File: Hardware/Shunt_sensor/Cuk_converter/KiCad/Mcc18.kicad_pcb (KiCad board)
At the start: 2 copper layers, 177.8 x 104.1 mm, 89 parts, among them Q1 IRFP4321PbF, U1 INA240, U2 DRIVER_(INEP), U3 LM7812_TO220, U4 Signals_MCC, U5 ZCS

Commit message: Finalized first version PCB
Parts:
- removed JP2: MosfetOn, Jumper:SolderJumper-2_P1.3mm_Open_TrianglePad1.0x1.5mm
- removed JP3: Diode On, Jumper:SolderJumper-2_P1.3mm_Open_Pad1.0x1.5mm
- removed Rg2: 10k, Resistor_SMD:R_0805_2012Metric_Pad1.15x1.40mm_HandSolder
- added JP5: ON/OFF, TerminalBlock:TerminalBlock_bornier-2_P5.08mm, F.Cu at (53.8, 40.6)
- added TP13: TP, TestPoint:TestPoint_Pad_2.0x2.0mm, B.Cu at (196.1, 145.3)
- added TP14: TP, TestPoint:TestPoint_Pad_2.0x2.0mm, F.Cu at (146.8, 113.3)
- C1: footprint Capacitor_SMD:C_0805_2012Metric_Pad1.15x1.40mm_HandSolder -> Capacitor_SMD:C_2512_6332Metric_Pad1.52x3.35mm_HandSolder; moved to B.Cu
- Cc10, Cc11, Cc12, Cc7, Cc8, Cc9, Ci1, Ci2, Ci3, Co1, Co2, Co3, Co4, Co5, HS1, L1/2, L2/2, Q1, R110, Tvs1, Tvs2, Tvs4, U1: moved to B.Cu
- Cs12, Cs13, Cs14, Cs15, Ds1, Ds2, Ds3, Ds4, F1, JP4, R103, R105, Rs2, Rs3, Rs4, Rs5: moved to F.Cu
- D1: footprint MCCplaca:TO-247-3_Horizontal_TabUp -> Package_TO_SOT_THT:TO-247-3_Horizontal_TabUp; moved to B.Cu
- JP1: value Diode On -> VBat-Sen
- L1, L3: footprint Inductor_SMD:L_0805_2012Metric_Pad1.15x1.40mm_HandSolder -> Jumper:SolderJumper-2_P1.3mm_Open_Pad1.0x1.5mm
- Rshunt1: footprint MCCplaca Shunt:PML100HZPJV0L5 -> MCCplaca:PML100HZPJV0L5; moved to B.Cu
- TP1, TP10, TP11, TP12, TP2, TP3, TP4, TP6, TP7, TP8, TP9: value TestPoint_Probe -> TP; footprint TestPoint:TestPoint_Pad_D1.0mm -> TestPoint:TestPoint_Pad_2.0x2.0mm
- TP5: value TestPoint_Probe -> TP; footprint TestPoint:TestPoint_Pad_D1.0mm -> TestPoint:TestPoint_Pad_2.0x2.0mm; moved to B.Cu
- U2: footprint MCCplaca:Driver_(INEP)_SMD -> MCCplaca:Driver_(INEP); moved to F.Cu
- U3: footprint MCCplaca:TO-220-3_Horizontal_TabDown_SMD -> MCCplaca:TO-220-3_Horizontal_TabDown; moved to F.Cu
- U4: footprint MCCplaca:SignalsBarrapinos_SMD -> MCCplaca:SignalsBarrapinosGrande; moved to B.Cu
- U5: footprint MCCplaca:ZCS18 -> MCCplaca:ZCS18_Handsoldering
- moved Tvs1 233.7 mm to (88.3, 57.8), turned to 180 degrees
- moved R105 225.5 mm to (184.8, 67.9), turned to 90 degrees
- moved JP4 224.1 mm to (188.0, 69.2), turned to 0 degrees
- moved Tvs2 223.4 mm to (89.9, 54.3)
- moved R102 222.4 mm to (188.0, 120.1), turned to 180 degrees
- moved C1 221.9 mm to (102.2, 49.5), turned to 90 degrees
- moved R103 221.3 mm to (187.5, 65.5), turned to 180 degrees
- moved R110 221.0 mm to (106.0, 52.6)
- moved R101 220.0 mm to (188.0, 123.4), turned to 180 degrees
- moved Tvs4 209.6 mm to (108.7, 102.2), turned to 90 degrees
- moved TP8 143.6 mm to (105.4, 112.4)
- moved TP12 135.8 mm to (177.2, 109.9)
- moved TP10 134.6 mm to (173.4, 113.0)
- moved TP9 132.7 mm to (110.5, 106.0)
- moved TP11 126.9 mm to (160.7, 104.8)
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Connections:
- net /HG renamed /Gate
- net /HS renamed /Source
- net Net-(F1-Pad2) renamed /-P_unfused
- C11 pad 1: GND -> GNDA
- C16 pad 2: GND -> GNDA
- D1 pad 1: Net-(D1-Pad1) -> /-B
- JP1 pad 1: Net-(D1-Pad1) -> /-B
- JP1 pad 2: /-B -> GND
- Tvs3 pad 2: GND -> GNDA
- U1 pad 2: GND -> GNDA
- U2 pad 3: /LG -> Net-(U2-Pad3)
- U2 pad 4: /-B -> GND
- U5 pad 2: Net-(U5-Pad2) -> GND
- U5 pad 4: Net-(U5-Pad4) -> GND
- U5 pad 6: Net-(U5-Pad6) -> GND
- U5 pad 8: Net-(U5-Pad8) -> GND
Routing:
- net /+Vp: track 506.7 -> 34.7 mm, vias 0 -> 1
- net /+B: track 425.0 -> 27.9 mm, vias 1 -> 5
- net /-B: track 472.2 -> 128.7 mm, vias 0 -> 1
- net GND: track 551.4 -> 236.3 mm, vias 4 -> 15
- net +5VA: track 17.0 -> 262.4 mm, vias 1 -> 3
- net /-Vp: track 248.7 -> 14.7 mm, vias 0 -> 6
- net /Source: track 245.1 -> 75.6 mm, vias 15 -> 0
- net /+18V_OUT: track 230.4 -> 72.9 mm, vias 1 -> 2
- net GNDA: track 376.3 -> 491.1 mm, vias 8 -> 6
- net +5V: track 107.9 -> 7.46 mm
- net Net-(JP5-Pad2): track 0.00 -> 92.2 mm, vias 0 -> 1
- net Net-(D1-Pad1): track 37.7 -> 0.00 mm
- net /Vbat_adc+: track 68.9 -> 31.5 mm, vias 2 -> 0
- net /Gate: track 10.3 -> 45.1 mm
- net /Vb_sen+: track 95.3 -> 127.4 mm
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- added copper zone on B.Cu, net (none)
- added copper zone on F.Cu, net (none)
- added copper zone on B.Cu, net /+B
- added copper zone on B.Cu, net /+Vp
- added copper zone on B.Cu, net /-B
- added copper zone on B.Cu, net /-P_unfused
- added copper zone on B.Cu, net /-Vp
- added copper zone on B.Cu, net /Rs-
- added copper zone on B.Cu, net /Source
- added copper zone on B.Cu, net GND
- added copper zone on B.Cu, net GNDA
- added copper zone on F.Cu, net GNDA
- removed copper zone on F.Cu, net /Rs-
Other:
- board size 177.8 x 104.1 mm -> 199.1 x 127.5 mm
- net class Alta tensao added: clearance 1.27, trace_width 0.508, via_dia 0.9, via_drill 0.7
- net class Default: clearance 0.295 -> 0.3048
- net class High Voltage removed
- net class INA added: clearance 0.3048, trace_width 0.3429, via_dia 0.9, via_drill 0.7
- rule pad_to_mask_clearance: 0 -> 0.2
- rule trace_clearance: 0.295 -> 0.3048
- rule trace_min: 0.0499 -> 0.0508

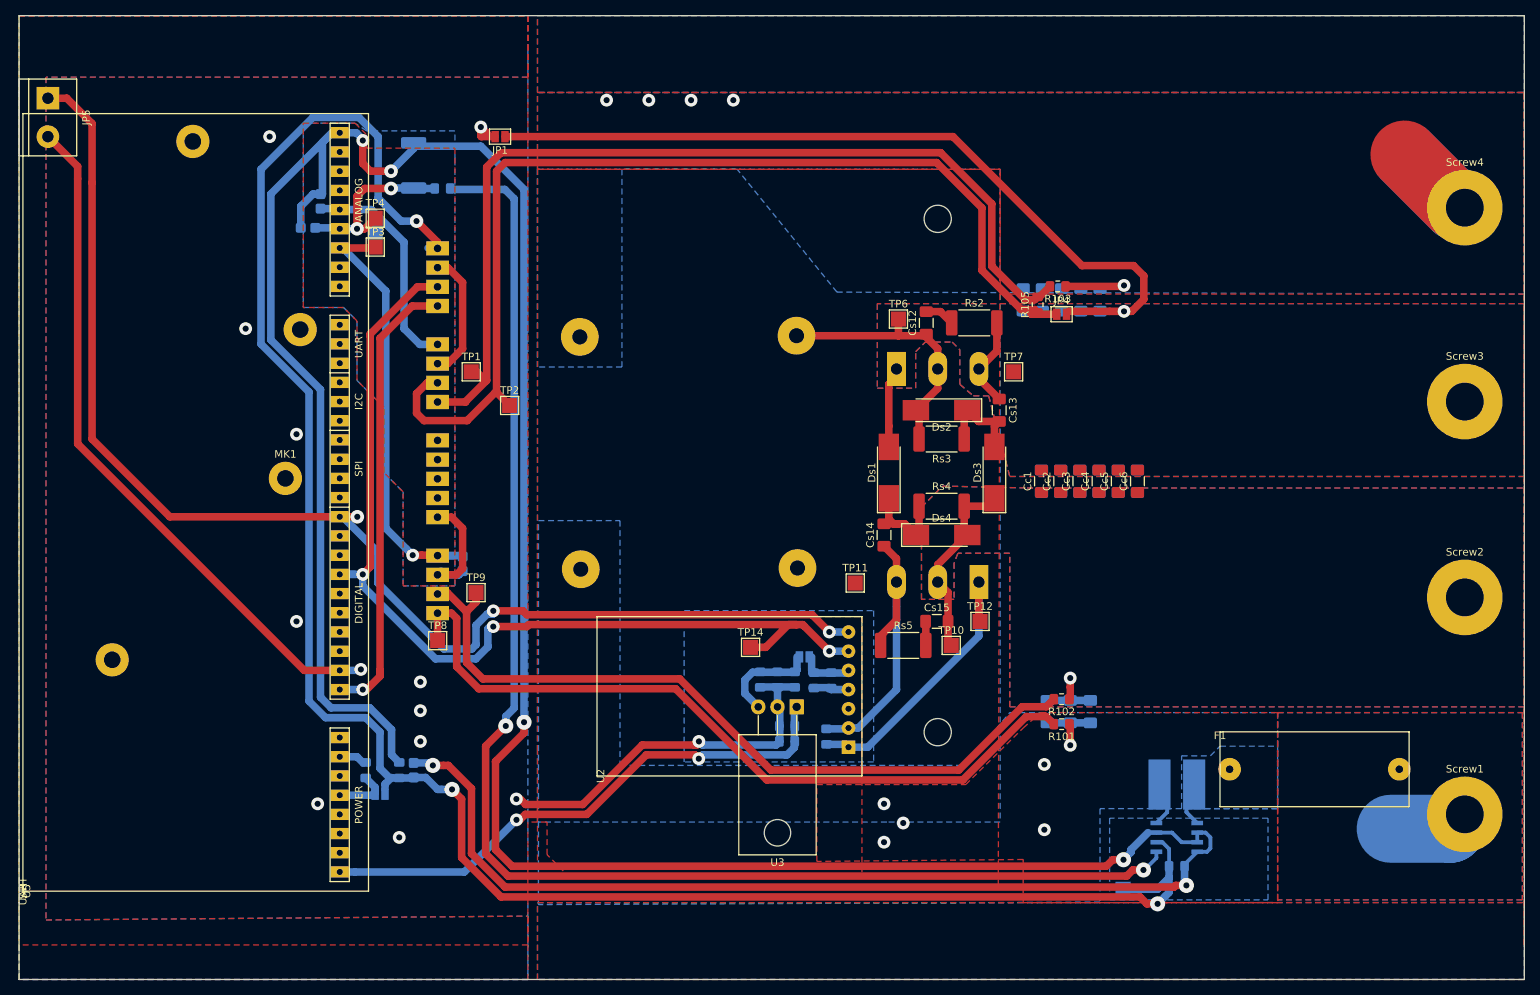
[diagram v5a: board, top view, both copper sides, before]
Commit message: final adjusted for cnc.
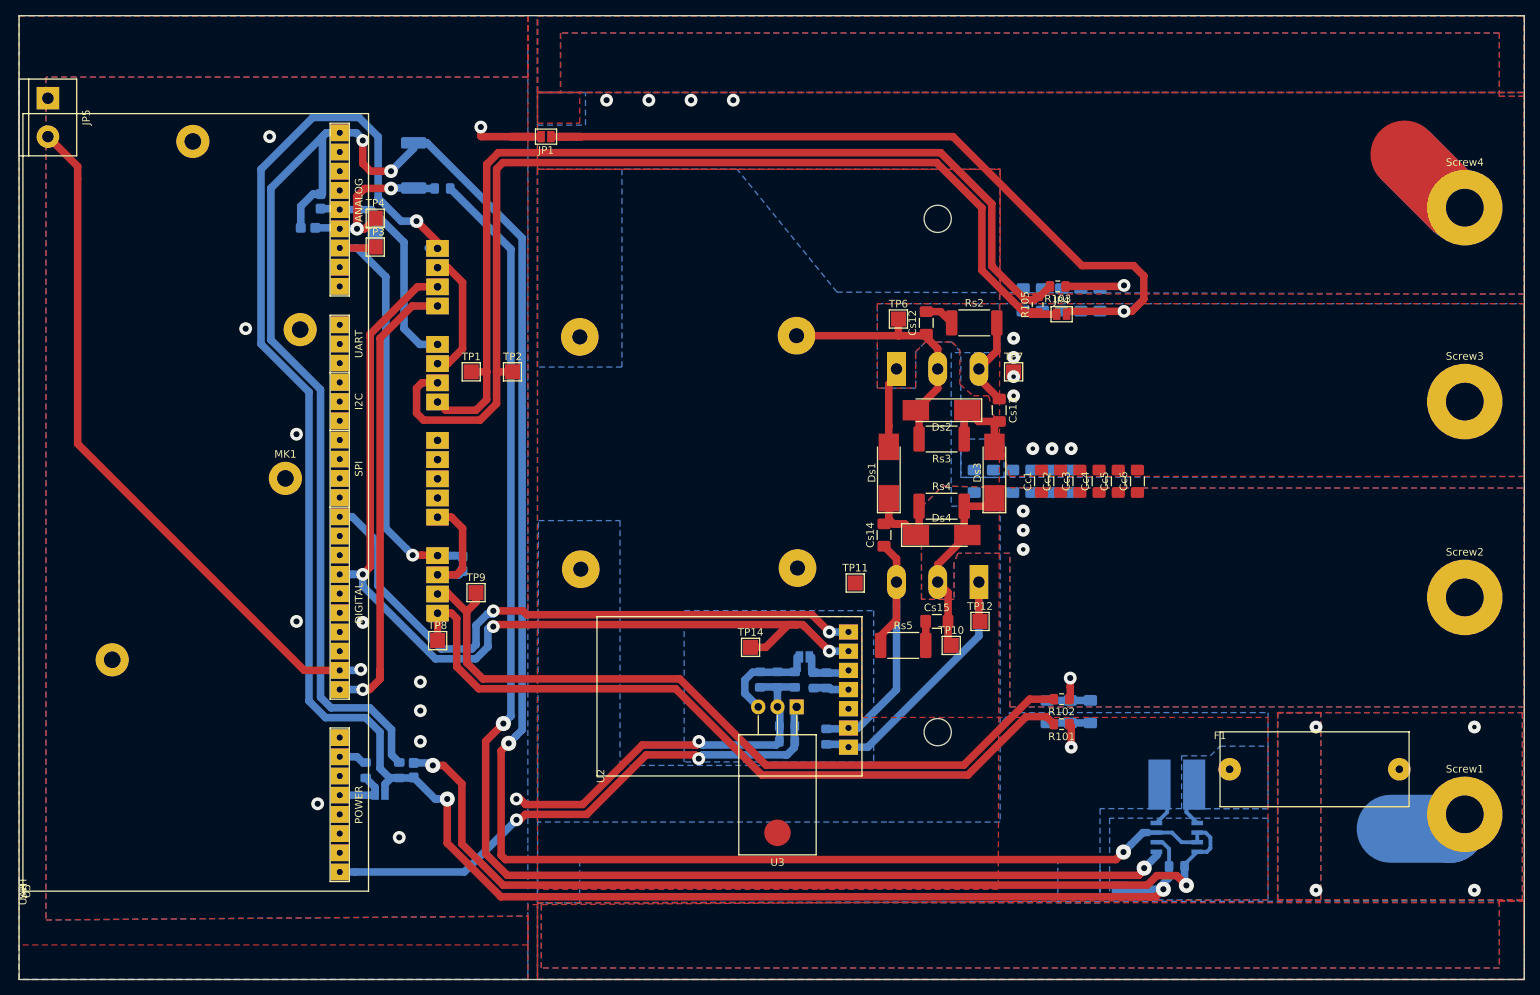
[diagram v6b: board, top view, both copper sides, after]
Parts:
- U2: footprint MCCplaca:Driver_(INEP) -> MCCplaca:Driver_(INEP)_PadClearence_12mil
- U4: footprint MCCplaca:SignalsBarrapinosGrande -> MCCplaca:SignalsBarrapinosGrande-Padclearnce12mil
- U5: footprint MCCplaca:ZCS18_Handsoldering -> MCCplaca:ZCS18_Handsoldering_Padclearence12mil
- moved Cc10 8.89 mm to (184.0, 91.3)
- moved Cc11 8.89 mm to (186.6, 91.3)
- moved Cc7 8.89 mm to (176.4, 91.3)
- moved Cc12 8.89 mm to (189.1, 91.3)
- moved Cc8 8.89 mm to (178.9, 91.3)
- moved Cc9 8.89 mm to (181.5, 91.3)
- moved JP1 6.08 mm to (119.7, 45.7)
- moved TP2 4.46 mm to (115.3, 76.8)
- moved C9 0.63 mm to (156.8, 117.7)
- moved TP13 0.51 mm to (195.6, 145.3)
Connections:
- C1 pad 2: GNDA -> GND
- C11 pad 1: GNDA -> GND
- C16 pad 2: GNDA -> GND
- Tvs1 pad 2: GNDA -> GND
- Tvs2 pad 2: GNDA -> GND
- Tvs3 pad 2: GNDA -> GND
- Tvs4 pad 1: GNDA -> GND
- U1 pad 2: GNDA -> GND
- U1 pad 3: GNDA -> GND
- U1 pad 4: GNDA -> GND
- U1 pad 7: GNDA -> GND
- U4 pad 12: GNDA -> GND
- U4 pad 16: GNDA -> GND
- U4 pad 3: GNDA -> GND
- U4 pad 5: GNDA -> GND
- U5 pad 37: GNDA -> GND
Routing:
- net GNDA: track 491.1 -> 0.00 mm, vias 6 -> 0
- net GND: track 236.3 -> 641.0 mm, vias 15 -> 21
- net /INA240_OUT: track 189.0 -> 184.3 mm
- net +5VA: track 262.4 -> 258.0 mm
- net /-B: track 128.7 -> 125.5 mm, vias 1 -> 8
- net /Vb_sen+: track 127.4 -> 129.5 mm
- net /Vpanel_adc+: track 59.0 -> 60.1 mm
- net /Vp_sen+: track 102.2 -> 101.7 mm
- net /-Vp: track 14.7 -> 15.2 mm, vias 6 -> 1
- net /Vp_sen-: track 102.3 -> 101.8 mm
- net /-P_unfused: vias 0 -> 4
- net /+Vp: vias 1 -> 4
- removed copper zone on F.Cu, net /-Vp
- removed copper zone on B.Cu, net GNDA
- removed copper zone on F.Cu, net GNDA
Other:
- net class INA removed

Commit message: Fixed signals tracks
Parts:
- Tvs4: moved to F.Cu
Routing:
- net /Vpanel_adc+: track 60.1 -> 57.7 mm
- net GND: track 641.0 -> 640.5 mm
- net /Vbat_adc+: track 31.5 -> 32.0 mm, vias 0 -> 1
